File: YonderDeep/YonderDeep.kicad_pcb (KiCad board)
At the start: 2 copper layers, 65 x 56 mm, 18 parts, among them J1 GPIO

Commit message: LED Resistor added
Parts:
- added Resistor1: R, Resistor_THT:R_Box_L8.4mm_W2.5mm_P5.08mm, F.Cu at (149.7, 54.1)
- moved LED1 5.12 mm to (159.1, 53.6), turned to -90 degrees
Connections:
- LED1 pad 1: LED_GPIO12 -> Net-(LED1-Pad1)
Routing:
- net LED_GPIO12: track 15.6 -> 9.19 mm
- net Net-(LED1-Pad1): track 0.00 -> 4.46 mm
- net Back_Motor: track 120.6 -> 121.7 mm
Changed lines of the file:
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@@
   (net 38 "Left_Motor")
   (net 39 "unconnected-(J1-Pad1)")
+  (net 40 "Net-(LED1-Pad1)")
   (footprint "MountingHole:MountingHole_2.7mm_M2.5" locked (layer "F.Cu")
     (at 161.5 47.5)
@@
     (pad "" np_thru_hole circle locked (at 0 0) (size 2.7 2.7) (drill 2.7) (layers *.Cu *.Mask))
   )
+  (footprint "Resistor_THT:R_Box_L8.4mm_W2.5mm_P5.08mm" (layer "F.Cu")
+    (at 149.72 54.07)
+    (descr "Resistor, Box series, Radial, pin pitch=5.08mm, 0.5W = 1/2W, length*width=8.38*2.54mm^2, http://www.vishay.com/docs/60051/cns020.pdf")
+    (tags "Resistor Box series Radial pin pitch 5.08mm 0.5W = 1/2W length 8.38mm width 2.54mm")
+    (property "Sheetfile" "YonderDeep.kicad_sch")
+    (property "Sheetname" "")
+    (attr through_hole)
+    (fp_text reference "Resistor1" (at 2.54 -2.52) (layer "User.1") hide
+      (effects (font (size 1 1) (thickness 0.15)))
+    )
+    (fp_text value "R" (at 2.54 2.52) (layer "F.Fab")
+      (effects (font (size 1 1) (thickness 0.15)))
+    )
+    (fp_text user "${REFERENCE}" (at 2.54 0) (layer "F.Fab")
+      (effects (font (size 1 1) (thickness 0.15)))
+    )
+    (fp_line (start -1.77 -1.39) (end 6.85 -1.39) (layer "F.SilkS") (width 0.12))
+    (fp_line (start 6.85 -1.39) (end 6.85 1.39) (layer "F.SilkS") (width 0.12))
+    (fp_line (start -1.77 1.39) (end 6.85 1.39) (layer "F.SilkS") (width 0.12))
+    (fp_line (start -1.77 -1.39) (end -1.77 1.39) (layer "F.SilkS") (width 0.12))
+    (fp_line (start 6.98 -1.52) (end -1.91 -1.52) (layer "F.CrtYd") (width 0.05))
+    (fp_line (start -1.91 1.52) (end 6.98 1.52) (layer "F.CrtYd") (width 0.05))
+    (fp_line (start 6.98 1.52) (end 6.98 -1.52) (layer "F.CrtYd") (width 0.05))
+    (fp_line (start -1.91 -1.52) (end -1.91 1.52) (layer "F.CrtYd") (width 0.05))
+    (fp_line (start 6.73 1.27) (end 6.73 -1.27) (layer "F.Fab") (width 0.1))
+    (fp_line (start 6.73 -1.27) (end -1.65 -1.27) (layer "F.Fab") (width 0.1))
+    (fp_line (start -1.65 -1.27) (end -1.65 1.27) (layer "F.Fab") (width 0.1))
+    (fp_line (start -1.65 1.27) (end 6.73 1.27) (layer "F.Fab") (width 0.1))
+    (pad "1" thru_hole circle (at 0 0) (size 1.6 1.6) (drill 0.8) (layers *.Cu *.Mask)
+      (net 35 "LED_GPIO12") (pintype "passive"))
+    (pad "2" thru_hole circle (at 5.08 0) (size 1.6 1.6) (drill 0.8) (layers *.Cu *.Mask)
+      (net 40 "Net-(LED1-Pad1)") (pintype "passive"))
+    (model "${KICAD6_3DMODEL_DIR}/Resistor_THT.3dshapes/R_Box_L8.4mm_W2.5mm_P5.08mm.wrl"
+      (offset (xyz 0 0 0))
+      (scale (xyz 1 1 1))
+      (rotate (xyz 0 0 0))
+    )
+  )
   (footprint "LED_THT:LED_D3.0mm" (layer "F.Cu")
-    (at 154.45 55.835 90)
+    (at 159.08 53.645 -90)
     (descr "LED, diameter 3.0mm, 2 pins")
     (tags "LED diameter 3.0mm 2 pins")
@@
     (fp_arc (start -0.23 -1.16619) (mid 3.17 0.000452) (end -0.230555 1.165476) (layer "F.Fab") (width 0.1))
     (fp_circle (center 1.27 0) (end 2.77 0) (layer "F.Fab") (width 0.1) (fill none))
-    (pad "1" thru_hole rect (at 0 0 90) (size 1.8 1.8) (drill 0.9) (layers *.Cu *.Mask)
-      (net 35 "LED_GPIO12") (pinfunction "Pin_1") (pintype "passive"))
-    (pad "2" thru_hole circle (at 2.54 0 90) (size 1.8 1.8) (drill 0.9) (layers *.Cu *.Mask)
+    (pad "1" thru_hole rect (at 0 0 270) (size 1.8 1.8) (drill 0.9) (layers *.Cu *.Mask)
+      (net 40 "Net-(LED1-Pad1)") (pinfunction "Pin_1") (pintype "passive"))
+    (pad "2" thru_hole circle (at 2.54 0 270) (size 1.8 1.8) (drill 0.9) (layers *.Cu *.Mask)
       (net 1 "GND") (pinfunction "Pin_2") (pintype "passive"))
     (model "${KICAD6_3DMODEL_DIR}/LED_THT.3dshapes/LED_D3.0mm.wrl"
@@
     (effects (font (size 1 1) (thickness 0.15)))
   )
-  (gr_text "-" (at 154.42 51.36 90) (layer "F.SilkS")
+  (gr_text "-" (at 157.16 56.89 90) (layer "F.SilkS")
     (effects (font (size 1 1) (thickness 0.15)))
   )
@@
     (effects (font (size 1 1) (thickness 0.15)))
   )
-  (gr_text "+" (at 154.4 57.56) (layer "F.SilkS")
+  (gr_text "+" (at 157.35 52.88) (layer "F.SilkS")
     (effects (font (size 1 1) (thickness 0.15)))
   )
@@
     (effects (font (size 2 2) (thickness 0.15)))
   )
-  (segment (start 128.58 96.84) (end 128.58 93.08) (width 0.3048) (layer "F.Cu") (net 2))
-  (segment (start 156.6124 90.091949) (end 156.6124 91.088051) (width 0.3048) (layer "F.Cu") (net 2))
-  (segment (start 136.808051 47.4324) (end 137.5124 46.728051) (width 0.3048) (layer "F.Cu") (net 2))
   (segment (start 155.140451 92.56) (end 129.1 92.56) (width 0.3048) (layer "F.Cu") (net 2))
-  (segment (start 155.908051 88.866749) (end 155.908051 89.3876) (width 0.3048) (layer "F.Cu") (net 2))
-  (segment (start 156.6124 91.088051) (end 155.140451 92.56) (width 0.3048) (layer "F.Cu") (net 2))
-  (segment (start 157.29 54.363838) (end 162.55 59.623838) (width 0.3048) (layer "F.Cu") (net 2))
-  (segment (start 122.2724 47.4324) (end 136.808051 47.4324) (width 0.3048) (layer "F.Cu") (net 2))
-  (segment (start 162.55 82.2248) (end 155.908051 88.866749) (width 0.3048) (layer "F.Cu") (net 2))
-  (segment (start 155.908051 89.3876) (end 156.6124 90.091949) (width 0.3048) (layer "F.Cu") (net 2))
-  (segment (start 155.4276 49.268051) (end 157.29 51.130451) (width 0.3048) (layer "F.Cu") (net 2))
-  (segment (start 162.55 59.623838) (end 162.55 82.2248) (width 0.3048) (layer "F.Cu") (net 2))
-  (segment (start 128.58 93.08) (end 129.11 92.55) (width 0.3048) (layer "F.Cu") (net 2))
-  (segment (start 155.4276 45.867149) (end 155.4276 49.268051) (width 0.3048) (layer "F.Cu") (net 2))
-  (segment (start 121.07 46.23) (end 122.2724 47.4324) (width 0.3048) (layer "F.Cu") (net 2))
-  (segment (start 157.29 51.130451) (end 157.29 54.363838) (width 0.3048) (layer "F.Cu") (net 2))
+  (segment (start 128.58 96.84) (end 128.58 93.08) (width 0.3048) (layer "F.Cu") (net 2))
   (segment (start 138.449549 44.93) (end 154.490451 44.93) (width 0.3048) (layer "F.Cu") (net 2))
   (segment (start 154.490451 44.93) (end 155.4276 45.867149) (width 0.3048) (layer "F.Cu") (net 2))
+  (segment (start 162.55 82.2248) (end 155.908051 88.866749) (width 0.3048) (layer "F.Cu") (net 2))
+  (segment (start 161.42 58.493838) (end 162.55 59.623838) (width 0.3048) (layer "F.Cu") (net 2))
   (segment (start 137.5124 45.867149) (end 138.449549 44.93) (width 0.3048) (layer "F.Cu") (net 2))
+  (segment (start 156.6124 90.091949) (end 156.6124 91.088051) (width 0.3048) (layer "F.Cu") (net 2))
+  (segment (start 155.4276 45.867149) (end 155.4276 49.268051) (width 0.3048) (layer "F.Cu") (net 2))
   (segment (start 137.5124 46.728051) (end 137.5124 45.867149) (width 0.3048) (layer "F.Cu") (net 2))
+  (segment (start 159.951945 52.012145) (end 161.42 53.4802) (width 0.3048) (layer "F.Cu") (net 2))
+  (segment (start 155.4276 49.268051) (end 158.171694 52.012145) (width 0.3048) (layer "F.Cu") (net 2))
+  (segment (start 161.42 53.4802) (end 161.42 58.493838) (width 0.3048) (layer "F.Cu") (net 2))
+  (segment (start 128.58 93.08) (end 129.11 92.55) (width 0.3048) (layer "F.Cu") (net 2))
+  (segment (start 122.2724 47.4324) (end 136.808051 47.4324) (width 0.3048) (layer "F.Cu") (net 2))
+  (segment (start 162.55 59.623838) (end 162.55 82.2248) (width 0.3048) (layer "F.Cu") (net 2))
+  (segment (start 155.908051 88.866749) (end 155.908051 89.3876) (width 0.3048) (layer "F.Cu") (net 2))
+  (segment (start 155.908051 89.3876) (end 156.6124 90.091949) (width 0.3048) (layer "F.Cu") (net 2))
+  (segment (start 156.6124 91.088051) (end 155.140451 92.56) (width 0.3048) (layer "F.Cu") (net 2))
+  (segment (start 136.808051 47.4324) (end 137.5124 46.728051) (width 0.3048) (layer "F.Cu") (net 2))
+  (segment (start 121.07 46.23) (end 122.2724 47.4324) (width 0.3048) (layer "F.Cu") (net 2))
+  (segment (start 158.171694 52.012145) (end 159.951945 52.012145) (width 0.3048) (layer "F.Cu") (net 2))
   (segment (start 123.85 90.08) (end 147.44 90.08) (width 0.3048) (layer "F.Cu") (net 3))
   (segment (start 147.44 90.08) (end 149.1524 91.7924) (width 0.3048) (layer "F.Cu") (net 3))
@@
   (segment (start 141.94 67.97) (end 151.04 77.07) (width 0.3048) (layer "B.Cu") (net 34))
   (segment (start 151.04 77.07) (end 151.04 96.87) (width 0.3048) (layer "B.Cu") (net 34))
-  (segment (start 149.925 55.835) (end 154.45 55.835) (width 0.3048) (layer "F.Cu") (net 35))
-  (segment (start 146.47 46.23) (end 147.75 47.51) (width 0.3048) (layer "F.Cu") (net 35))
-  (segment (start 147.75 53.66) (end 149.925 55.835) (width 0.3048) (layer "F.Cu") (net 35))
-  (segment (start 147.75 47.51) (end 147.75 53.66) (width 0.3048) (layer "F.Cu") (net 35))
+  (segment (start 147.75 51.25) (end 147.75 52.1) (width 0.3048) (layer "F.Cu") (net 35))
+  (segment (start 147.75 52.1) (end 149.72 54.07) (width 0.3048) (layer "F.Cu") (net 35))
+  (segment (start 147.74 47.5) (end 147.74 51.24) (width 0.3048) (layer "F.Cu") (net 35))
+  (segment (start 146.47 46.23) (end 147.74 47.5) (width 0.3048) (layer "F.Cu") (net 35))
+  (segment (start 147.74 51.24) (end 147.75 51.25) (width 0.3048) (layer "F.Cu") (net 35))
   (segment (start 139.66 96.84) (end 140.19 96.84) (width 0.3048) (layer "B.Cu") (net 38))
   (segment (start 115.99 48.77) (end 115.99 73.17) (width 0.3048) (layer "B.Cu") (net 38))
   (segment (start 115.99 73.17) (end 139.66 96.84) (width 0.3048) (layer "B.Cu") (net 38))
+  (segment (start 158.655 54.07) (end 159.08 53.645) (width 0.3048) (layer "F.Cu") (net 40))
+  (segment (start 154.8 54.07) (end 158.655 54.07) (width 0.3048) (layer "F.Cu") (net 40))
   (zone (net 1) (net_name "GND") (layer "B.Cu") (name "GND") (hatch edge 0.508)
     (connect_pads (clearance 0))

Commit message: Added signature
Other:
- board text added: "Revised by Christina Mai & Anurag Jadhav"
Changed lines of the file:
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@@
   (gr_line (start 100 81) (end 100 97) (layer "Edge.Cuts") (width 0.1))
   (gr_line (start 162 44) (end 103 44) (layer "Edge.Cuts") (width 0.1))
+  (gr_text "Revised by Christina Mai & Anurag Jadhav" (at 131.14 71.33) (layer "B.SilkS")
+    (effects (font (size 1 1) (thickness 0.15)) (justify mirror))
+  )
   (gr_text "GND\n" (at 160.72 64.61 90) (layer "F.SilkS")
     (effects (font (size 1 1) (thickness 0.15)))

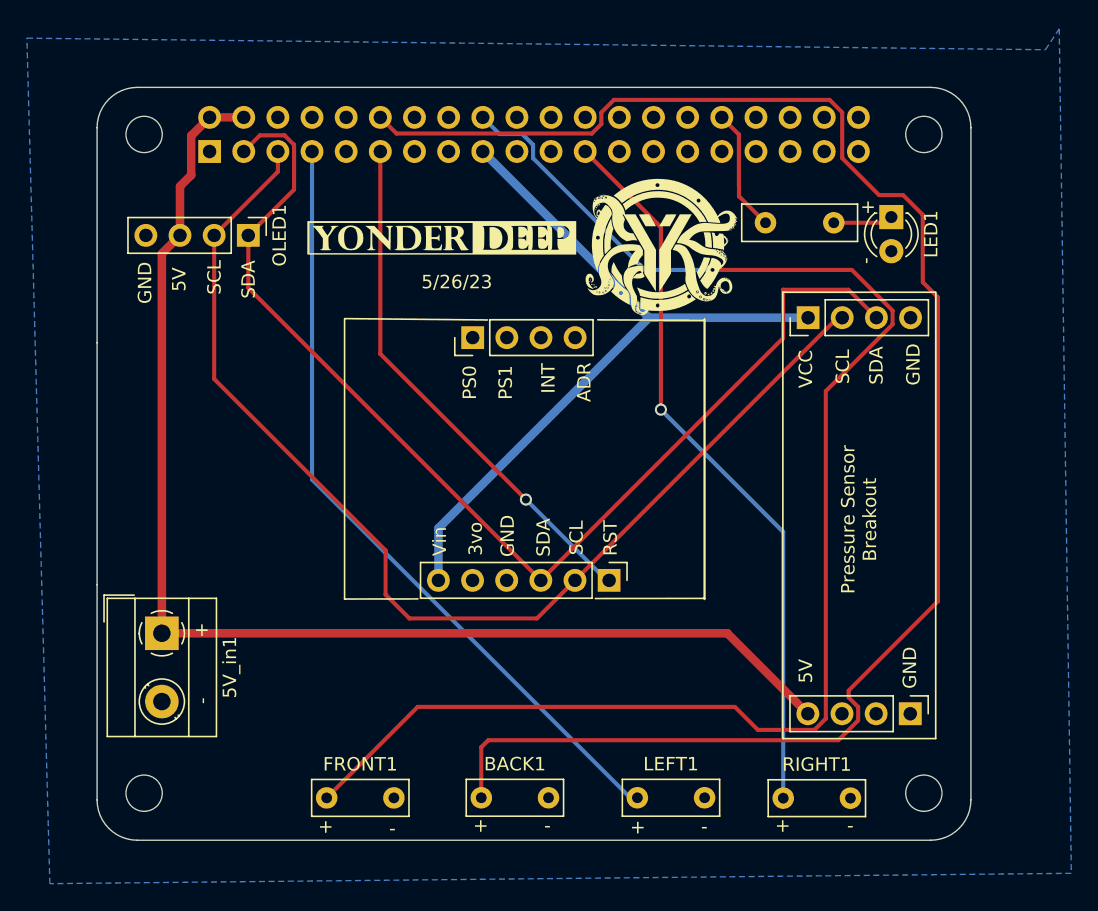
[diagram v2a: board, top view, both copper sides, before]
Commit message: Update
PCB update IMU pin footprint and new labels
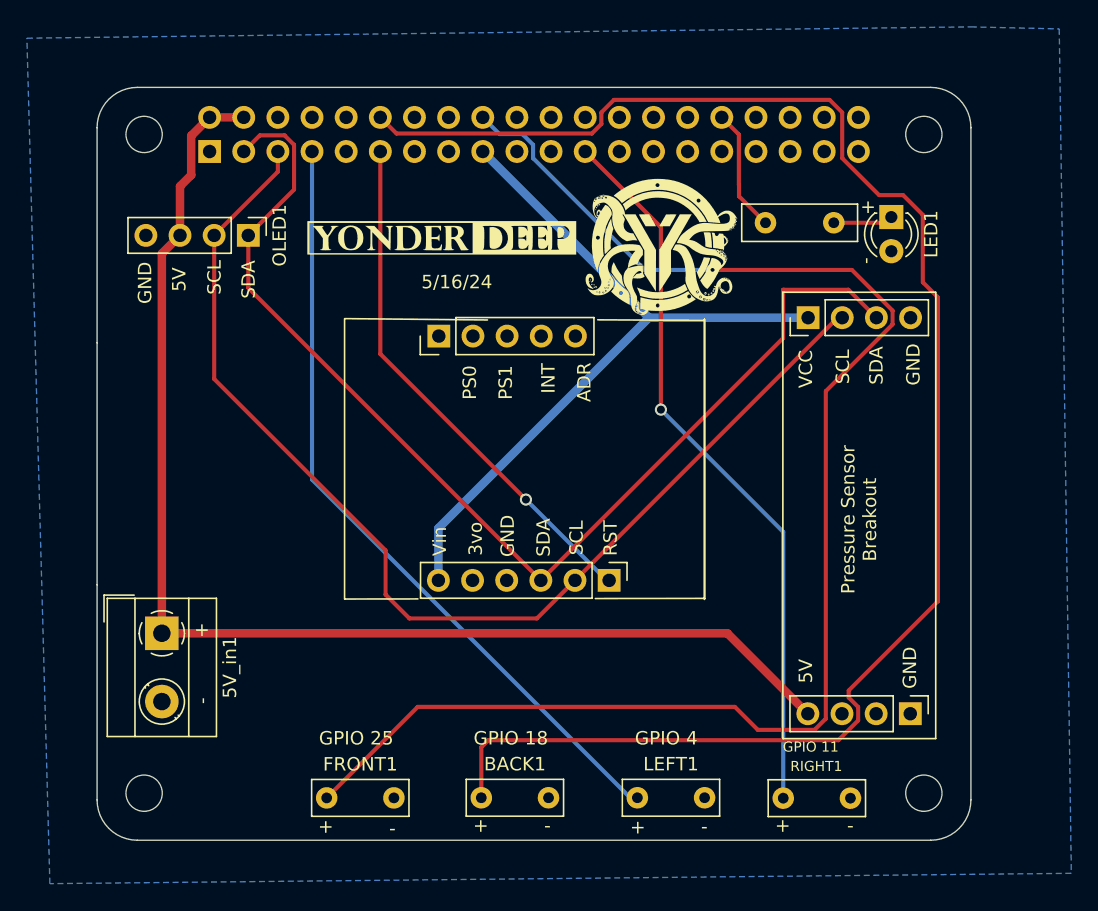
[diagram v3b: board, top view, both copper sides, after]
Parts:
- IMU_Right1: value Conn_01x04_Female -> Conn_01x05_Female; footprint Connector_PinHeader_2.54mm:PinHeader_1x04_P2.54mm_Vertical -> Connector_PinHeader_2.54mm:PinHeader_1x05_P2.54mm_Vertical
- moved IMU_Right1 2.52 mm to (125.4, 62.5)
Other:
- board text added: "5/16/24"
- board text added: "GPIO 11"
- board text added: "GPIO 18"
- board text added: "GPIO 25"
- board text added: "GPIO 4"
- board text added: "Revised by Alan Ye, Rebecca Fellbaum"
- board text removed: "5/26/23"
- board text removed: "Revised by Christina Mai & Anurag Jadhav"
